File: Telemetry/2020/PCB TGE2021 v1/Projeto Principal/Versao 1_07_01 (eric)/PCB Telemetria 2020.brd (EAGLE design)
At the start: 160 x 75.2 mm, 54 parts, among them IC1 INA240A1DR, IC2 MCP3221A6T-E_OTVAO, IC3 AZ1117IH-3.3TRG1, IC4 ACS758LCB-050B-PFF-T, IC5 ADS1115IDGSR, IC6 ACS712-030B3, IC7 THVD2410DR, IC8 TMP235AEDCKRQ1, J1 172042-0406, J2 43045-0412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

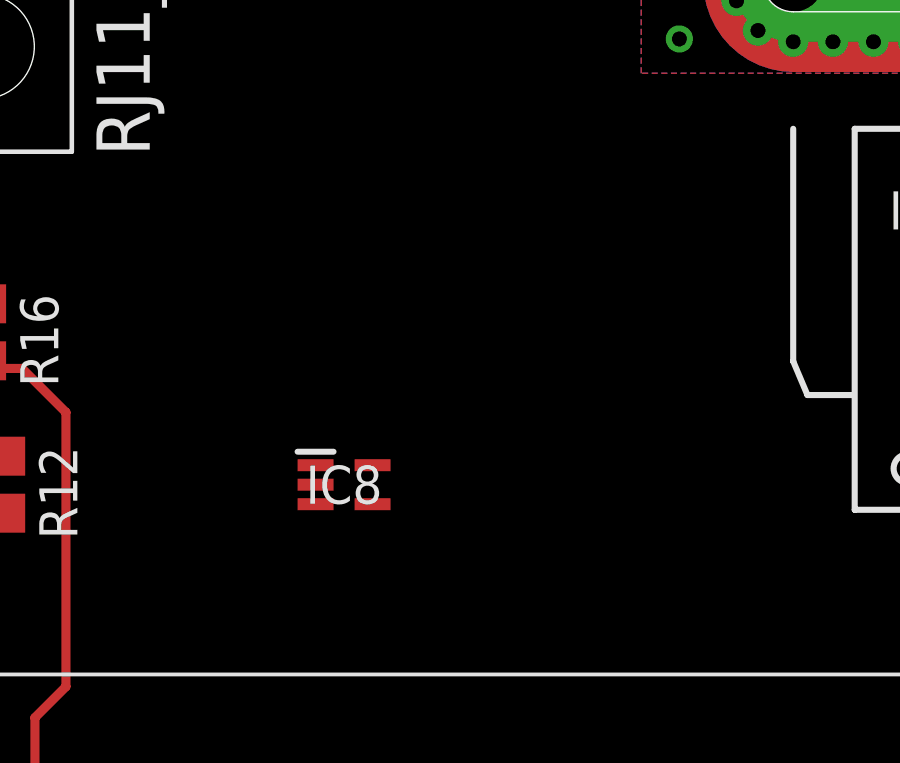
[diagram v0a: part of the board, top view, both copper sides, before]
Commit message: Uploading TMP235 wiring
Extra connectors without wiring, that's the reason for V1.07.01
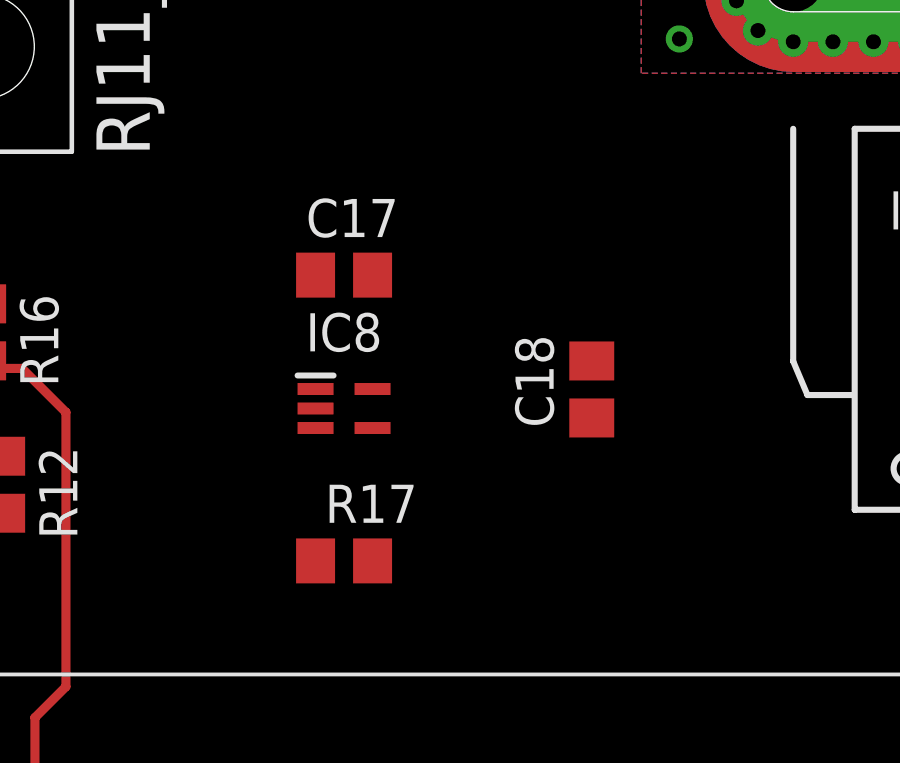
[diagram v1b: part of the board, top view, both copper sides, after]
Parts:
- added C17: 100nF, rcl:C0805
- added C18: 680pF, rcl:C0805
- added R17: 4.7k, rcl:R0805
- moved IC8 2.54 mm to (27.3, 43.8)
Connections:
- removed net N$11: U$1.14
- new net N$3: IC8.3, R17.1
- new net TMP_ADC2_8: C18.1, R17.2, U$1.14
- net GND: now also C17.2, C18.2, IC8.2
- net VCC_3V3: now also C17.1, IC8.4
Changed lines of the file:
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@@
 <?xml version="1.0" encoding="utf-8"?>
 <!DOCTYPE eagle SYSTEM "eagle.dtd">
-<eagle version="9.5.2">
+<eagle version="9.6.2">
 <drawing>
 <settings>
@@
 </layers>
 <board>
-<fusionsync huburn="a.cGVyc29uYWw6dWUyZDkwMWJh" projecturn="a.cGVyc29uYWw6dWUyZDkwMWJhIzIwMjAwODE2MzIzOTA5MTA2" f3durn="urn:adsk.wipprod:dm.lineage:uE01plevSWODFXVH0NNS5w" pcbguid="52094770-dfe4-426a-9aa2-8b08af3b6d69" lastpulledtime="" lastsyncedchangeguid="81b568d7-5ed1-2049-b759-ae446f31c16f"/>
+<fusionsync huburn="a.cGVyc29uYWw6dWUyZDkwMWJh" projecturn="a.cGVyc29uYWw6dWUyZDkwMWJhIzIwMjAwODE2MzIzOTA5MTA2" f3durn="urn:adsk.wipprod:dm.lineage:uE01plevSWODFXVH0NNS5w" pcbguid="52094770-dfe4-426a-9aa2-8b08af3b6d69" lastpulledtime="" lastsyncedchangeguid="81b568d7-5ed1-2049-b759-ae446f31c16f" latestrevisionid="" lastsyncedrevisionid="" lastboardhashguid="" lastpushedtime="" linktopcb3d="false"/>
 <plain>
 <wire x1="0" y1="0" x2="160" y2="0" width="0" layer="20"/>
@@
 <attribute name="VALUE" x="146.103" y="5.778" size="1.27" layer="27" align="center"/>
 </element>
-<element name="IC8" library="SamacSys_Parts" package="SOT65P210X110-5N" value="TMP235AEDCKRQ1" x="27.305" y="41.275" smashed="yes">
-<attribute name="DESCRIPTION" value="Board Mount Temperature Sensors Automotive grade, +/-0.5C analog output temperature sensor with 10 mV/C gain 5-SC70 -40 to 150" x="27.305" y="41.275" size="1.778" layer="27" display="off"/>
-<attribute name="HEIGHT" value="1.1mm" x="27.305" y="41.275" size="1.778" layer="27" display="off"/>
-<attribute name="MANUFACTURER_NAME" value="Texas Instruments" x="27.305" y="41.275" size="1.778" layer="27" display="off"/>
-<attribute name="MANUFACTURER_PART_NUMBER" value="TMP235AEDCKRQ1" x="27.305" y="41.275" size="1.778" layer="27" display="off"/>
-<attribute name="MOUSER_PART_NUMBER" value="595-TMP235AEDCKRQ1" x="27.305" y="41.275" size="1.778" layer="27" display="off"/>
-<attribute name="MOUSER_PRICE-STOCK" value="https://www.mouser.co.uk/ProductDetail/Texas-Instruments/TMP235AEDCKRQ1?qs=T3oQrply3y86j8c6PmMwyA%3D%3D" x="27.305" y="41.275" size="1.778" layer="27" display="off"/>
-<attribute name="NAME" x="27.305" y="41.275" size="1.27" layer="25" align="center"/>
-<attribute name="VALUE" x="27.305" y="41.275" size="1.27" layer="27" align="center"/>
+<element name="IC8" library="SamacSys_Parts" package="SOT65P210X110-5N" value="TMP235AEDCKRQ1" x="27.305" y="43.815" smashed="yes">
+<attribute name="DESCRIPTION" value="Board Mount Temperature Sensors Automotive grade, +/-0.5C analog output temperature sensor with 10 mV/C gain 5-SC70 -40 to 150" x="27.305" y="43.815" size="1.778" layer="27" display="off"/>
+<attribute name="HEIGHT" value="1.1mm" x="27.305" y="43.815" size="1.778" layer="27" display="off"/>
+<attribute name="MANUFACTURER_NAME" value="Texas Instruments" x="27.305" y="43.815" size="1.778" layer="27" display="off"/>
+<attribute name="MANUFACTURER_PART_NUMBER" value="TMP235AEDCKRQ1" x="27.305" y="43.815" size="1.778" layer="27" display="off"/>
+<attribute name="MOUSER_PART_NUMBER" value="595-TMP235AEDCKRQ1" x="27.305" y="43.815" size="1.778" layer="27" display="off"/>
+<attribute name="MOUSER_PRICE-STOCK" value="https://www.mouser.co.uk/ProductDetail/Texas-Instruments/TMP235AEDCKRQ1?qs=T3oQrply3y86j8c6PmMwyA%3D%3D" x="27.305" y="43.815" size="1.778" layer="27" display="off"/>
+<attribute name="NAME" x="27.305" y="46.355" size="1.27" layer="25" align="center"/>
+<attribute name="VALUE" x="27.305" y="43.815" size="1.27" layer="27" align="center"/>
+</element>
+<element name="C17" library="rcl" library_urn="urn:adsk.eagle:library:334" package="C0805" package3d_urn="urn:adsk.eagle:package:23617/2" value="100nF" x="27.305" y="48.26" smashed="yes">
+<attribute name="NAME" x="26.035" y="49.53" size="1.27" layer="25"/>
+<attribute name="POPULARITY" value="63" x="27.305" y="48.26" size="1.778" layer="27" display="off"/>
+<attribute name="SPICEPREFIX" value="C" x="27.305" y="48.26" size="1.778" layer="27" display="off"/>
+<attribute name="VALUE" x="26.035" y="45.72" size="1.27" layer="27"/>
+</element>
+<element name="R17" library="rcl" library_urn="urn:adsk.eagle:library:334" package="R0805" package3d_urn="urn:adsk.eagle:package:23553/2" value="4.7k" x="27.305" y="38.735" smashed="yes">
+<attribute name="NAME" x="26.67" y="40.005" size="1.27" layer="25"/>
+<attribute name="POPULARITY" value="85" x="27.305" y="38.735" size="1.778" layer="27" display="off"/>
+<attribute name="SPICEPREFIX" value="R" x="27.305" y="38.735" size="1.778" layer="27" display="off"/>
+<attribute name="VALUE" x="26.67" y="36.195" size="1.27" layer="27"/>
+</element>
+<element name="C18" library="rcl" library_urn="urn:adsk.eagle:library:334" package="C0805" package3d_urn="urn:adsk.eagle:package:23617/2" value="680pF" x="35.56" y="44.45" smashed="yes" rot="R90">
+<attribute name="NAME" x="34.29" y="43.18" size="1.27" layer="25" rot="R90"/>
+<attribute name="POPULARITY" value="63" x="35.56" y="44.45" size="1.778" layer="27" rot="R90" display="off"/>
+<attribute name="SPICEPREFIX" value="C" x="35.56" y="44.45" size="1.778" layer="27" rot="R90" display="off"/>
+<attribute name="VALUE" x="38.1" y="43.18" size="1.27" layer="27" rot="R90"/>
 </element>
 </elements>
@@
 <contactref element="C16" pad="2"/>
 <contactref element="RJ11_1" pad="P$3"/>
+<contactref element="IC8" pad="2"/>
+<contactref element="C17" pad="2"/>
+<contactref element="C18" pad="2"/>
 <wire x1="139.7" y1="48.089" x2="139.7" y2="53.511" width="0" layer="19" extent="1-1"/>
 <wire x1="140.142" y1="45.212" x2="139.7" y2="48.089" width="0" layer="19" extent="1-1"/>
@@
 <wire x1="49.337" y1="34.036" x2="56.007" y2="32.07" width="0" layer="19" extent="1-1"/>
 <wire x1="49.276" y1="36.639" x2="49.337" y2="34.036" width="0" layer="19" extent="1-1"/>
-<wire x1="92.71" y1="23.81" x2="94.676" y2="46.355" width="0" layer="19" extent="1-1"/>
-<wire x1="97.155" y1="23.81" x2="92.71" y2="23.81" width="0" layer="19" extent="1-1"/>
-<wire x1="22.2" y1="30.95" x2="49.337" y2="34.036" width="0" layer="19" extent="1-1"/>
-<wire x1="15.24" y1="47.305" x2="22.2" y2="30.95" width="0" layer="19" extent="1-1"/>
+<wire x1="35.56" y1="45.4" x2="49.276" y2="36.639" width="0" layer="19" extent="1-1"/>
+<wire x1="28.255" y1="48.26" x2="35.56" y2="45.4" width="0" layer="19" extent="1-1"/>
+<wire x1="26.355" y1="43.815" x2="28.255" y2="48.26" width="0" layer="19" extent="1-1"/>
+<wire x1="15.24" y1="47.305" x2="26.355" y2="43.815" width="0" layer="19" extent="1-1"/>
 <wire x1="5.544" y1="46.355" x2="15.24" y2="47.305" width="0" layer="19" extent="1-1"/>
 <wire x1="5.08" y1="38.42" x2="5.544" y2="46.355" width="0" layer="19" extent="1-1"/>
+<wire x1="22.2" y1="30.95" x2="26.355" y2="43.815" width="0" layer="19" extent="1-1"/>
 <wire x1="12.065" y1="64.775" x2="15.24" y2="47.305" width="0" layer="19" extent="1-1"/>
 <wire x1="20.32" y1="66.82" x2="12.065" y2="64.775" width="0" layer="19" extent="1-1"/>
 <wire x1="2.54" y1="66.82" x2="12.065" y2="64.775" width="0" layer="19" extent="1-1"/>
+<wire x1="92.71" y1="23.81" x2="94.676" y2="46.355" width="0" layer="19" extent="1-1"/>
+<wire x1="97.155" y1="23.81" x2="92.71" y2="23.81" width="0" layer="19" extent="1-1"/>
 <wire x1="37.8" y1="6.05" x2="22.2" y2="30.95" width="0" layer="19" extent="1-1"/>
 </signal>
@@
 <wire x1="5.08" y1="40.32" x2="5.08" y2="42.081" width="0.508" layer="1"/>
 <wire x1="5.08" y1="42.081" x2="5.544" y2="42.545" width="0.508" layer="1"/>
+<contactref element="IC8" pad="4"/>
+<contactref element="C17" pad="1"/>
 <wire x1="138.43" y1="48.089" x2="138.43" y2="53.511" width="0" layer="19" extent="1-1"/>
 <wire x1="138.242" y1="45.212" x2="138.43" y2="48.089" width="0" layer="19" extent="1-1"/>
@@
 <wire x1="35.2" y1="30.95" x2="47.437" y2="34.036" width="0" layer="19" extent="1-1"/>
 <wire x1="24.8" y1="30.95" x2="35.2" y2="30.95" width="0" layer="19" extent="1-1"/>
-<wire x1="15.875" y1="40.325" x2="24.8" y2="30.95" width="0" layer="19" extent="1-1"/>
+<wire x1="28.255" y1="43.165" x2="24.8" y2="30.95" width="0" layer="19" extent="1-1"/>
+<wire x1="15.875" y1="40.325" x2="28.255" y2="43.165" width="0" layer="19" extent="1-1"/>
 <wire x1="11.43" y1="38.42" x2="15.875" y2="40.325" width="0" layer="19" extent="1-1"/>
 <wire x1="5.08" y1="40.32" x2="11.43" y2="38.42" width="0" layer="19" extent="1-1"/>
 <wire x1="9.525" y1="64.775" x2="5.544" y2="42.545" width="0" layer="19" extent="1-1"/>
+<wire x1="26.355" y1="48.26" x2="5.08" y2="40.32" width="0" layer="19" extent="1-1"/>
 </signal>
 <signal name="MSHUNT_AMP">
@@
 <contactref element="U$1" pad="25"/>
 </signal>
-<signal name="N$11">
+<signal name="TMP_ADC2_8">
 <contactref element="U$1" pad="14"/>
+<contactref element="R17" pad="2"/>
+<contactref element="C18" pad="1"/>
+<wire x1="28.255" y1="38.735" x2="35.56" y2="43.5" width="0" layer="19" extent="1-1"/>
+<wire x1="30" y1="6.05" x2="28.255" y2="38.735" width="0" layer="19" extent="1-1"/>
 </signal>
 <signal name="N$12">
@@
 <wire x1="13.335" y1="62.23" x2="20.32" y2="62.72" width="0" layer="19" extent="1-1"/>
 </signal>
+<signal name="N$3">
+<contactref element="R17" pad="1"/>
+<contactref element="IC8" pad="3"/>
+<wire x1="26.355" y1="38.735" x2="26.355" y2="43.165" width="0" layer="19" extent="1-1"/>
+</signal>
 </signals>
